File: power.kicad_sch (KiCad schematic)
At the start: 35 parts, among them Q2 AO3400A, U8 SIC431AED-T1-GE3, U9 TPS564247DRLR

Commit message: [#3] Re-annotate schematic
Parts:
- renumbered C36 to C1, C45 to C10, C46 to C11, C47 to C12, C48 to C13, C49 to C14, C50 to C15, C51 to C16, C52 to C17, C53 to C18, C54 to C19, C37 to C2, C55 to C20, C38 to C3, C39 to C4, C40 to C5, C41 to C6, C42 to C7, C43 to C8, C44 to C9, Q2 to Q1, R54 to R1, R60 to R10, R86 to R2, R55 to R3, R56 to R4, R57 to R5, R58 to R6, R84 to R7, R85 to R8, R59 to R9, U8 to U1, U9 to U2

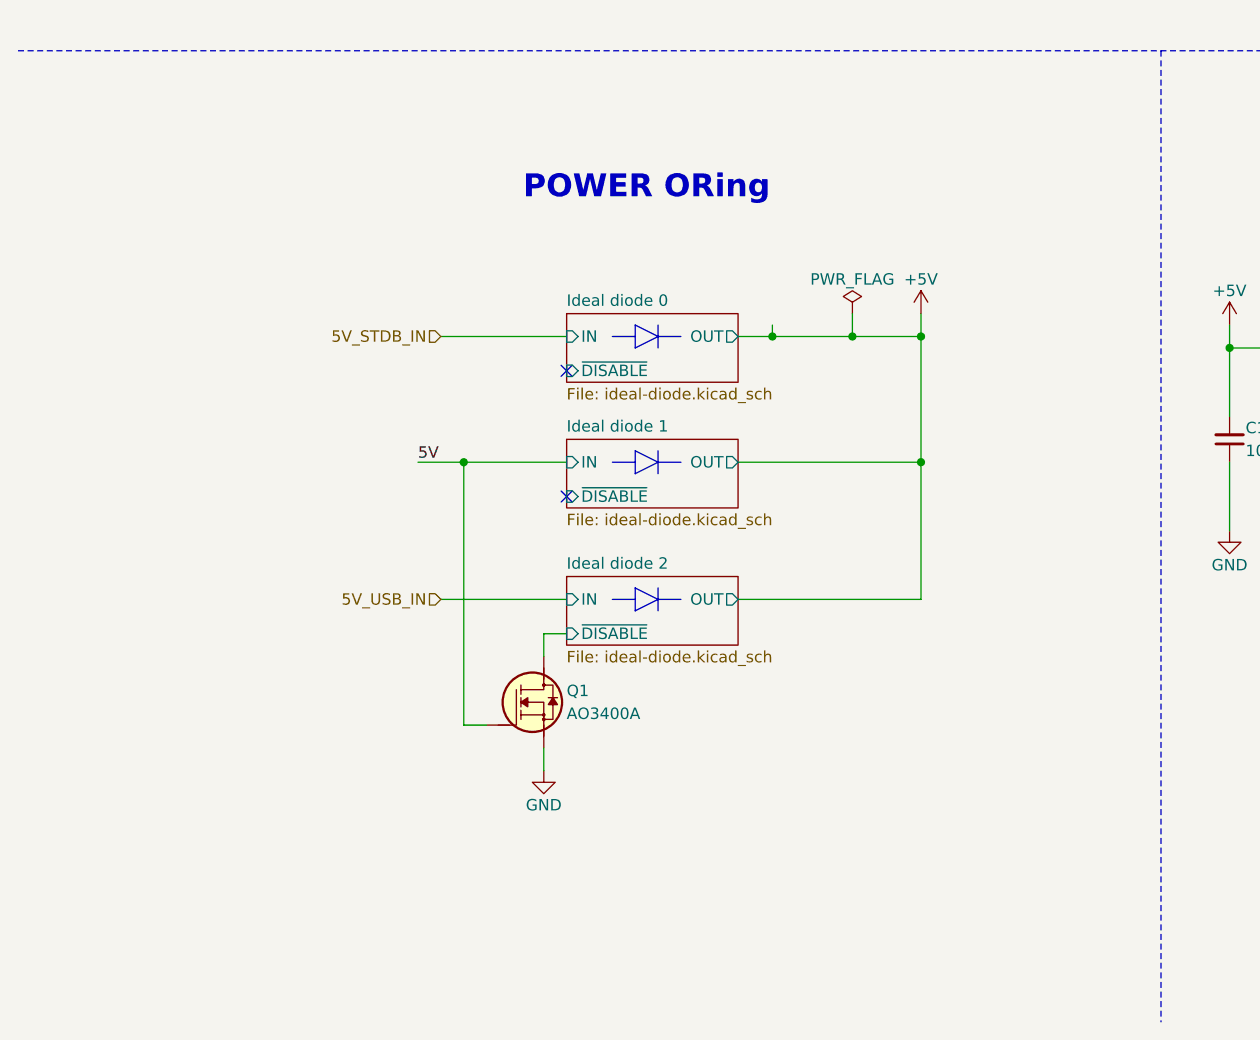
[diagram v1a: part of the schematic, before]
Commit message: [#3] Add 5V and 3V3 power indicator LEDs and test-points
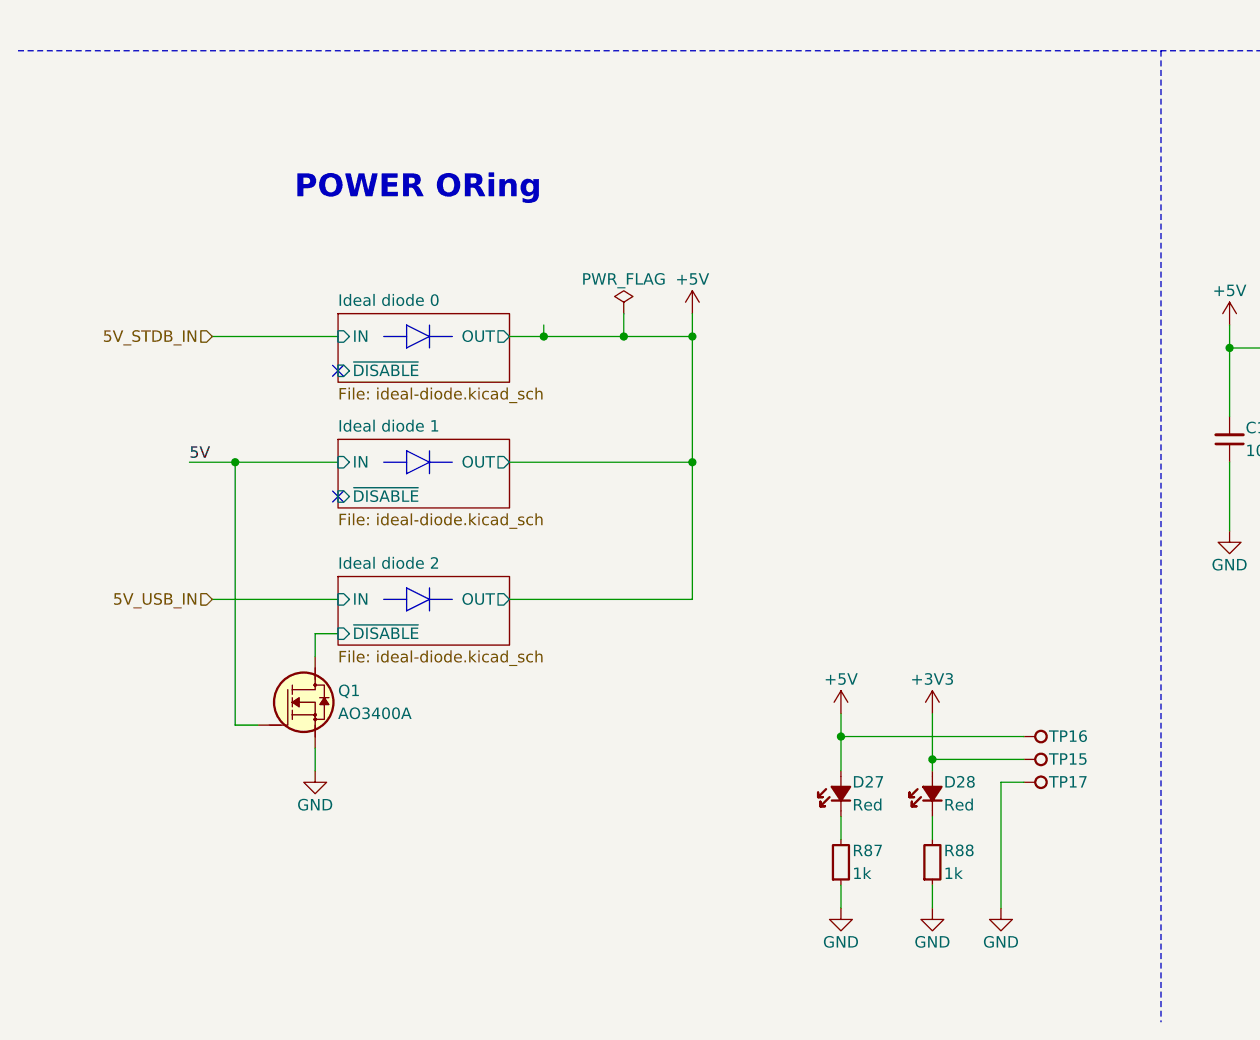
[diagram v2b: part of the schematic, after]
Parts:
- added D27, D28: LED-R-0603_KT-0603R, DW-footprints:LED_0603_1608Metric_R, symbol DW-diodes:LED-R-0603_KT-0603R
- added R87, R88: R-1k-0402, DW-footprints:R_0402_1005Metric, symbol DW-resistors:R-1k-0402
- added TP15, TP16, TP17: TP_SMD_0.75mm, DW-footprints:TP_SMD_0.75mm, symbol DW-test-points:TP_SMD_0.75mm
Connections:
- net +3V3: now also D28.2 (A), TP15.1
- net +5V: now also D27.2 (A), TP16.1
- net GND: now also R87.1, R88.1, TP17.1
- new net: D27.1 (C), R87.2
- new net: D28.1 (C), R88.2
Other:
- moved on the sheet: Q1
